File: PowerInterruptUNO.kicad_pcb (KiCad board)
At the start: 2 copper layers, 68.6 x 53.3 mm, 51 parts, among them J1 Power, J10 6P6C, J11 USB_C_Receptacle_USB2.0, J12 Screw_Terminal_01x02, J13 USB_A_Vertical, J14 Screw_Terminal_01x02, J2 Analog, J3 Barrel_Jack_Switch_SMT, J4 Screw_Terminal_01x06, J5 Screw_Terminal_01x06, J6 Screw_Terminal_01x03, J7 Screw_Terminal_01x02, J8 Digital/PWM, J9 Digital/PWM, Q1 MMBT3904, Q2 TIP42, U1 LM317_TO-220

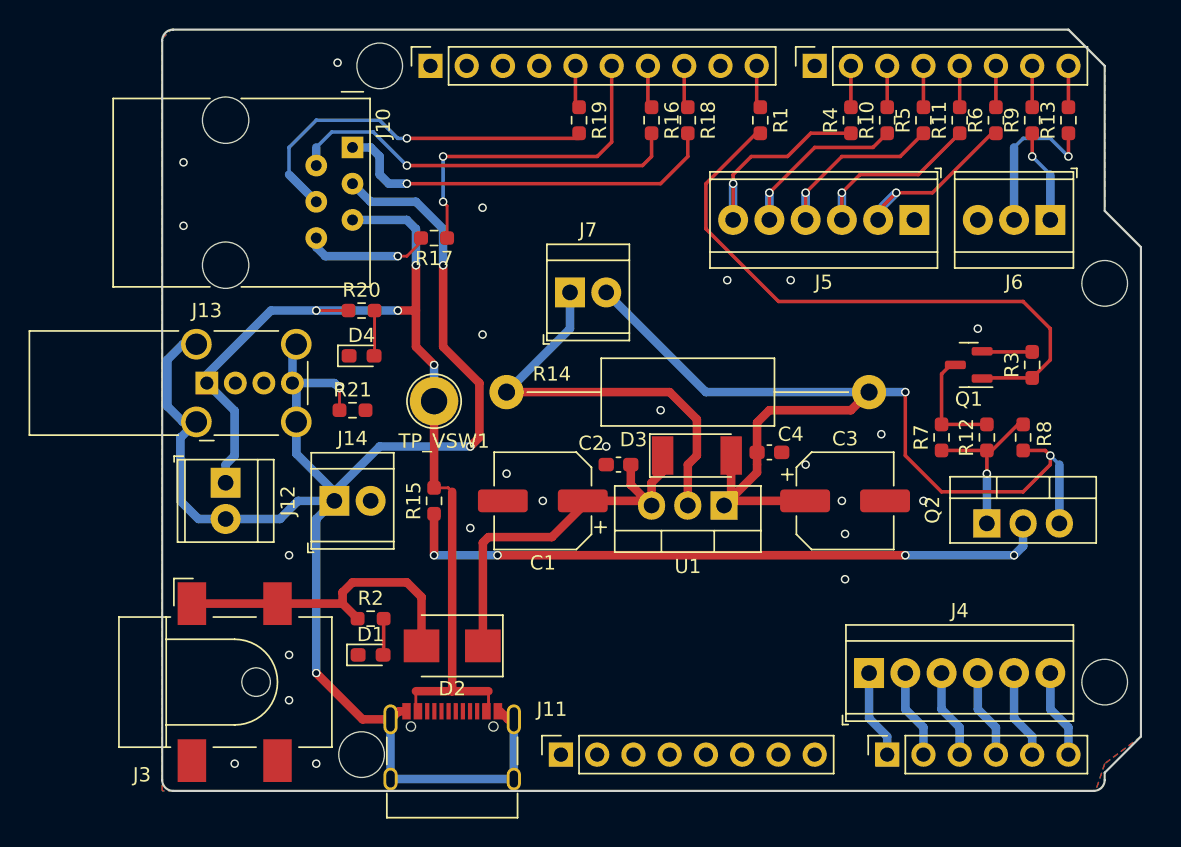
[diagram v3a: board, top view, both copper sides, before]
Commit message: Prior to moving J11 inboard
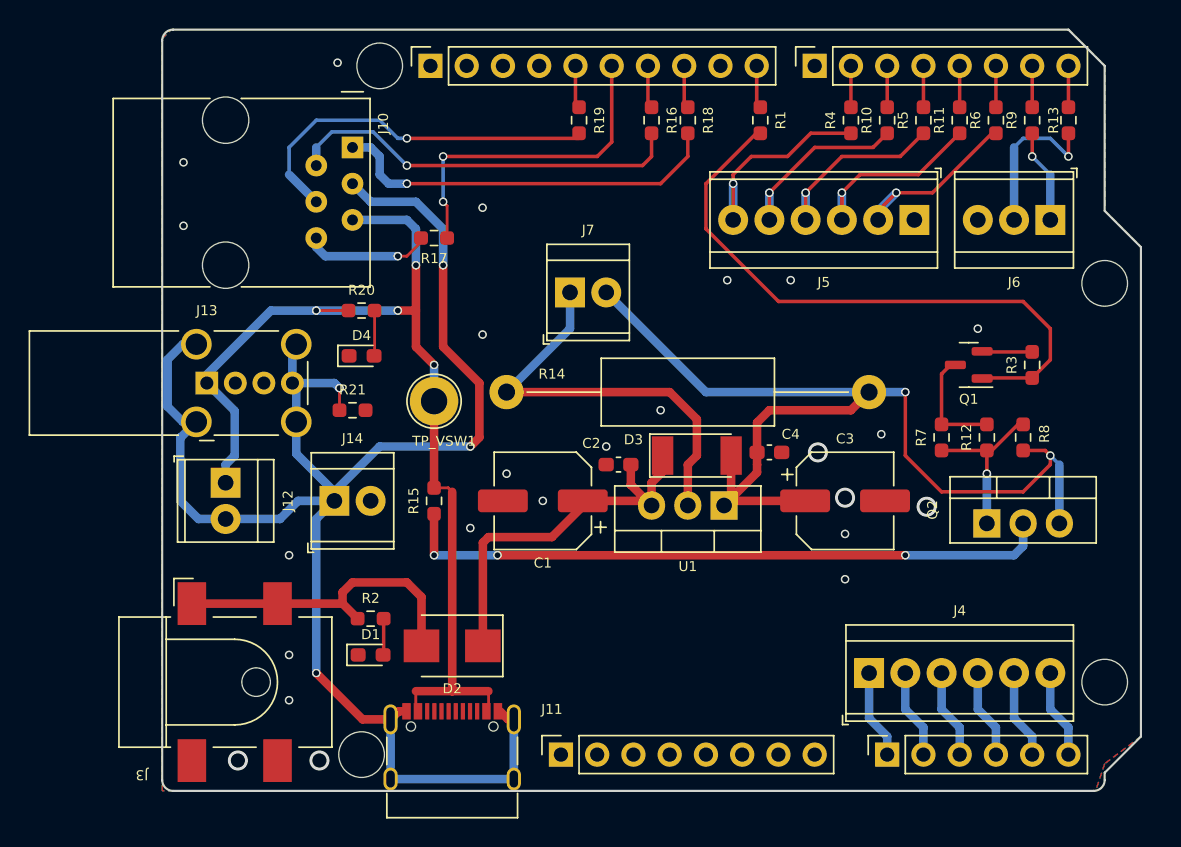
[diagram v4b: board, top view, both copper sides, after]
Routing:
- net Net-(Q2-Pad2): vias 4 -> 3

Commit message: Move J11. Change text size. Move a few other parts to help with text placement. Add visa to stich ground. DRC error related to double pads on J11 I can not clear. Do not think it is a problem (he foolishly types).
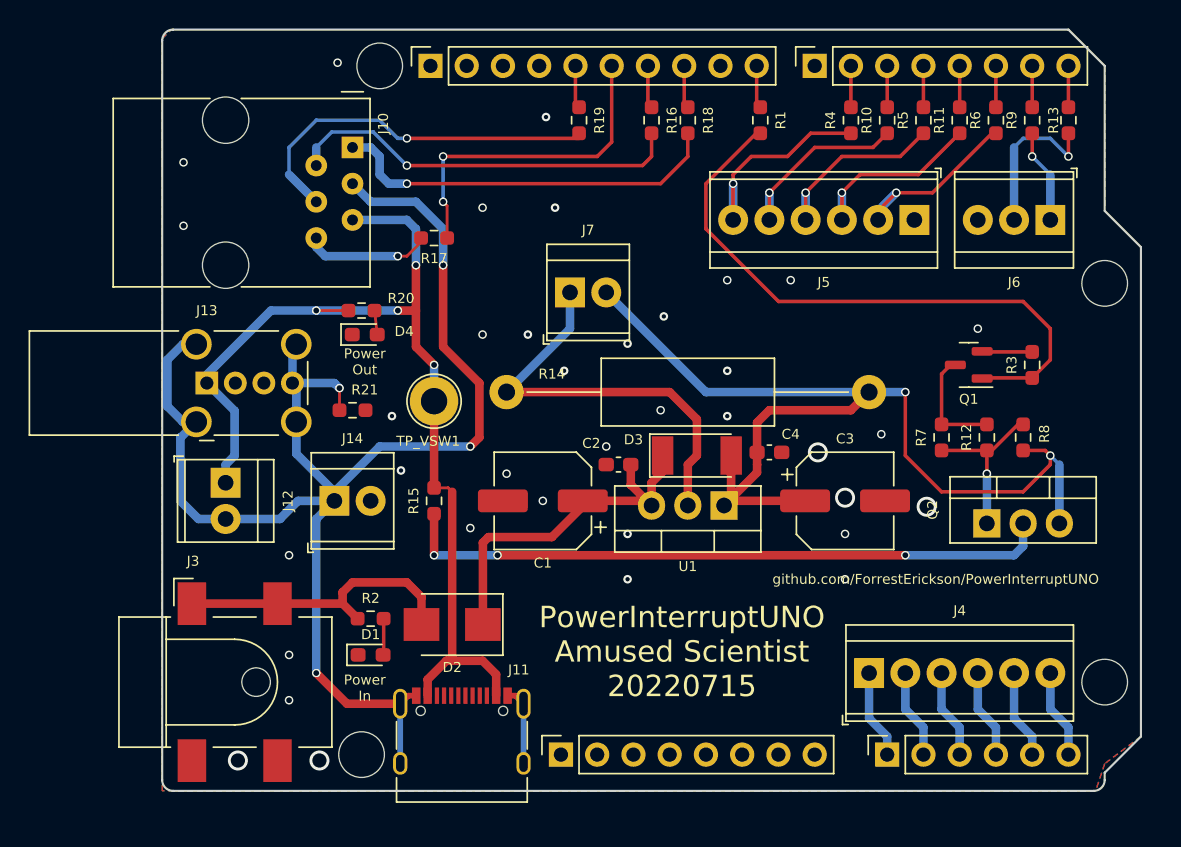
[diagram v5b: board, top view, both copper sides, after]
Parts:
- moved D4 1.51 mm to (114.2, 68.0)
- moved D2 1.49 mm to (120.3, 88.3)
- moved J11 1.29 mm to (121.0, 97.0)
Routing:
- net Net-(J10-Pad3): track 117.0 -> 109.2 mm
- net +VSW: track 74.1 -> 72.4 mm
- net Net-(D4-Pad2): track 3.19 -> 1.69 mm
- net +9V: track 22.5 -> 21.0 mm
- net Net-(C1-Pad1): track 27.9 -> 26.4 mm
- net GND: vias 24 -> 36
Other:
- board text added: "Power In"
- board text added: "Power Out"
- board text added: "PowerInterruptUNO Amused Scientist 20220715"
- board text added: "github.com/ForrestErickson/PowerInterruptUNO"
